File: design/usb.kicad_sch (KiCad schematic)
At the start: 24 parts, among them J4 USB_B_Mini, SW1 RST, U7 74AHC1G08, U8 USBLC6-2SC6, U9 FT231XS

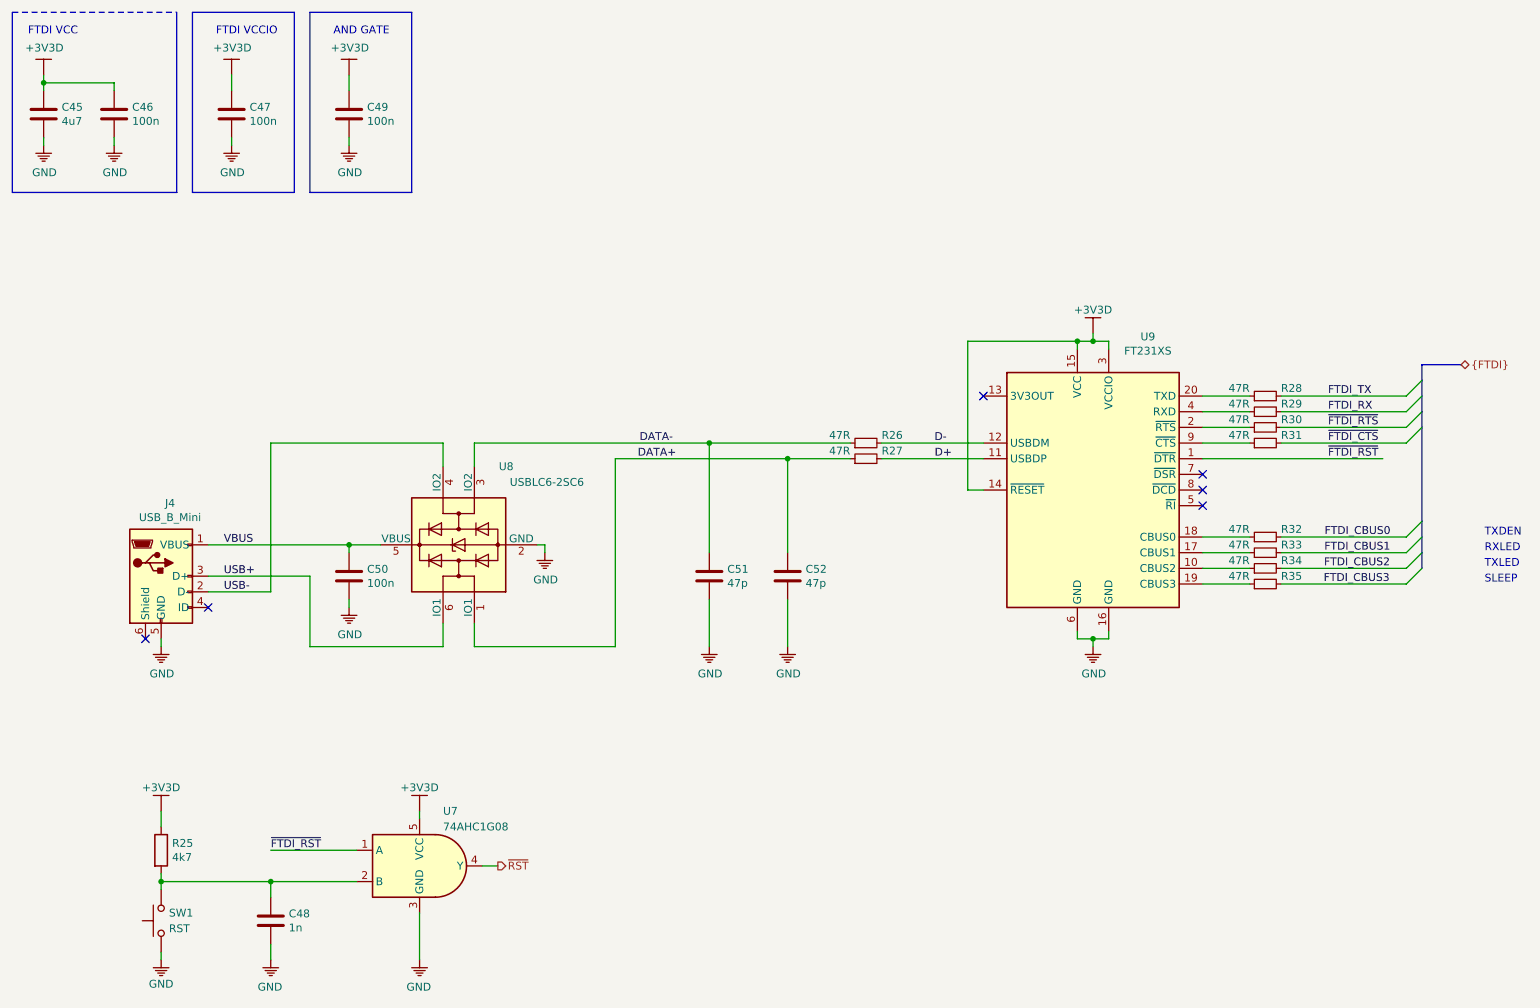
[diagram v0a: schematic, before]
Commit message: Named button reset net
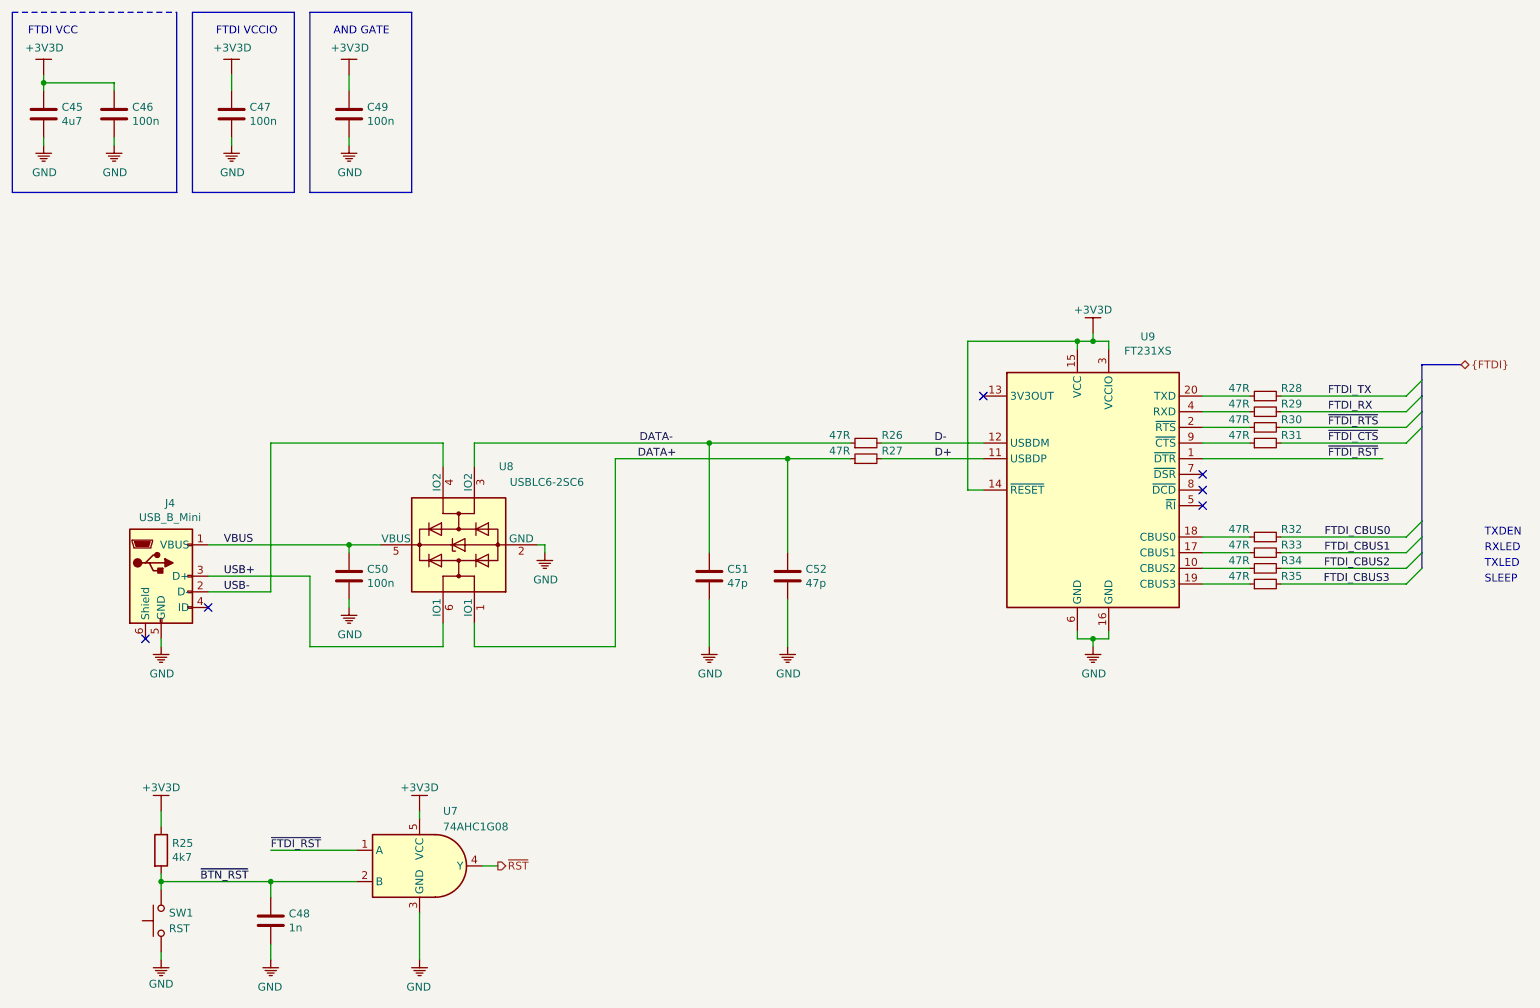
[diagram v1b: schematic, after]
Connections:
- net ~BTN_RST: now reaches C48.1, R25.2, SW1.2, U7.2 (B)
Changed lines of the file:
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@@
   (junction (at 190.5 68.58))
   (junction (at 190.5 116.84))
-  (no_connect (at 208.28 95.25))
+  (no_connect (at 36.83 116.84))
   (no_connect (at 208.28 90.17))
+  (no_connect (at 208.28 92.71))
   (no_connect (at 46.99 111.76))
   (no_connect (at 172.72 77.47))
-  (no_connect (at 208.28 92.71))
-  (no_connect (at 36.83 116.84))
+  (no_connect (at 208.28 95.25))
   (bus_entry (at 241.3 77.47) (size 2.54 -2.54))
   (bus_entry (at 241.3 80.01) (size 2.54 -2.54))
@@
   (wire (pts (xy 220.98 105.41) (xy 241.3 105.41)))
   (wire (pts (xy 220.98 107.95) (xy 241.3 107.95)))
-  (bus (pts (xy 243.84 72.39) (xy 243.84 74.93)))
+  (bus (pts (xy 243.84 72.39) (xy 243.84 77.47)))
   (bus (pts (xy 243.84 72.39) (xy 250.19 72.39)))
-  (bus (pts (xy 243.84 74.93) (xy 243.84 80.01)))
+  (bus (pts (xy 243.84 77.47) (xy 243.84 80.01)))
   (bus (pts (xy 243.84 80.01) (xy 243.84 97.79)))
   (bus (pts (xy 243.84 97.79) (xy 243.84 102.87)))
@@
     (effects (font (size 1.27 1.27)) (justify left bottom))
   )
+  (label "~BTN_RST" (at 45.72 156.21 0)
+    (effects (font (size 1.27 1.27)) (justify left bottom))
+  )

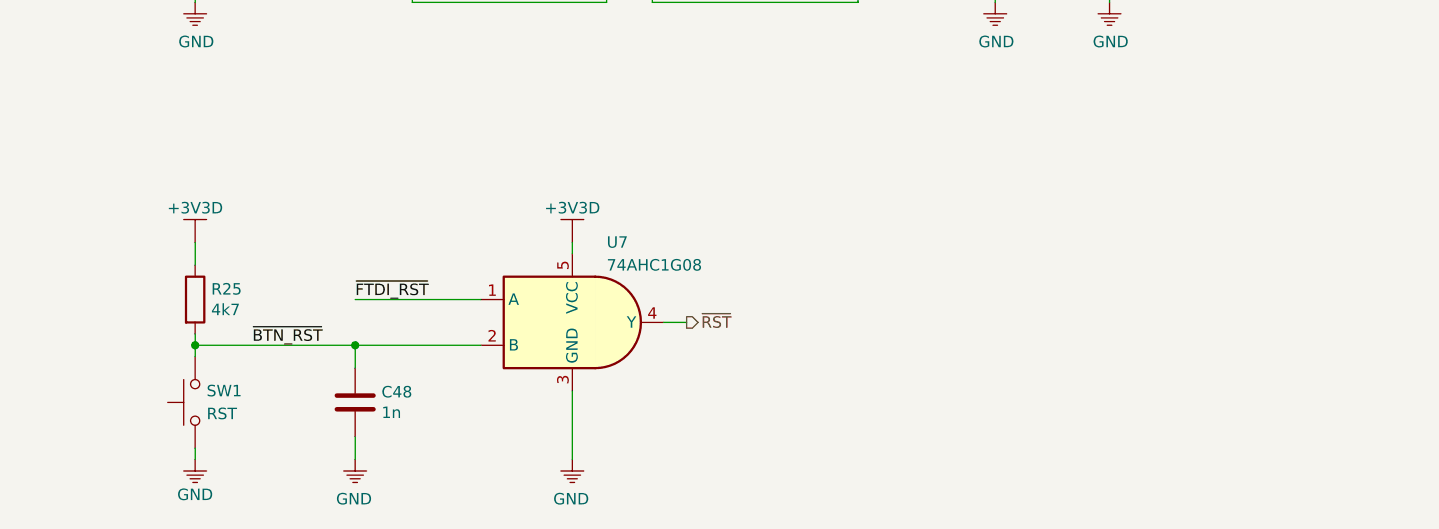
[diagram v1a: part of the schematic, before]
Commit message: Updated reset system
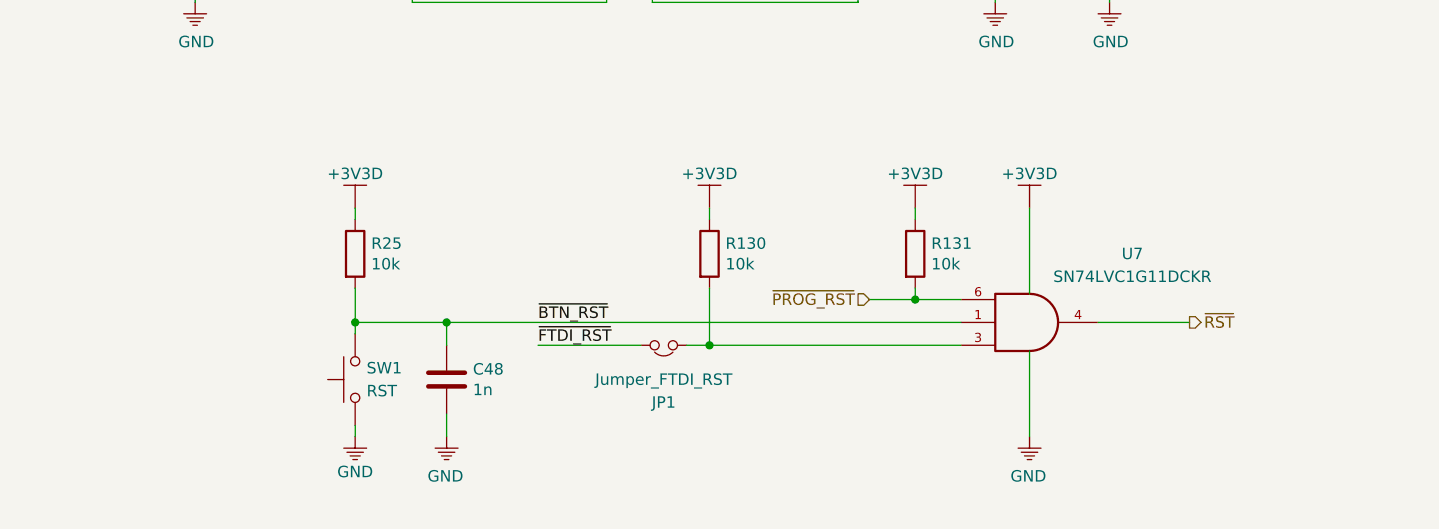
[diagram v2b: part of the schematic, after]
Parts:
- removed U7: 74AHC1G08, Package_TO_SOT_SMD:SOT-23-5, symbol KLIB_Logic:74AHC1G08
- added JP1: Jumper_FTDI_RST, Connector_PinHeader_2.54mm:PinHeader_1x02_P2.54mm_Vertical, symbol Device:Jumper_NC_Small
- added R130, R131: 10k, Resistor_SMD:R_0603_1608Metric, symbol Device:R
- added U7: SN74LVC1G11DCKR, Package_TO_SOT_SMD:SOT-363_SC-70-6, symbol 74xGxx:74LVC1G11
- R25: value 4k7 -> 10k
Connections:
- net +3V3D: now also R130.1, R131.1, U7.5 (VCC)
- net GND: now also U7.2 (GND)
- net ~BTN_RST: now also U7.1
- net ~FTDI_RST: now also JP1.1
- net ~RST: now also U7.4
- new net: JP1.2, R130.2, U7.3
- new net ~PROG_RST: R131.2, U7.6
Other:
- moved on the sheet: C48, R25, SW1
